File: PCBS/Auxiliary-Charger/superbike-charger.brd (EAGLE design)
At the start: 100 x 80 mm, 20 parts, among them U1 BQ24125RHLR

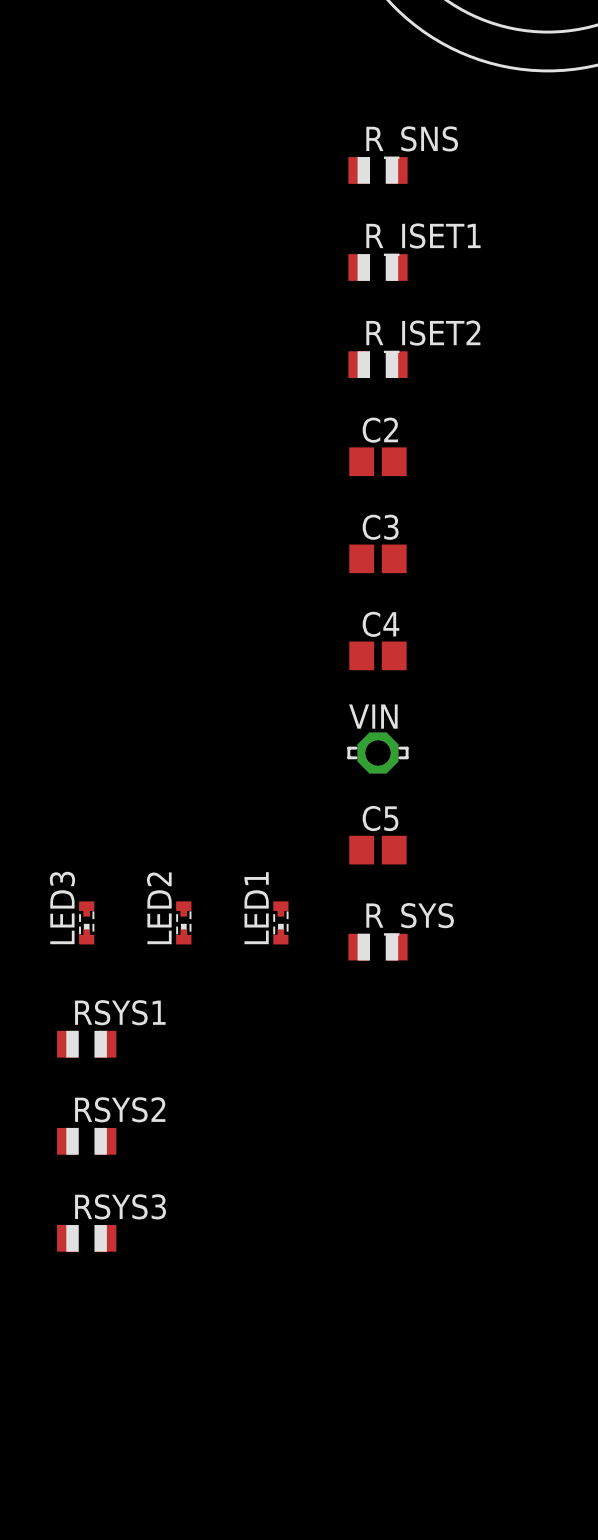
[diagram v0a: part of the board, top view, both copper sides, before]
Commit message: teensy board final draft
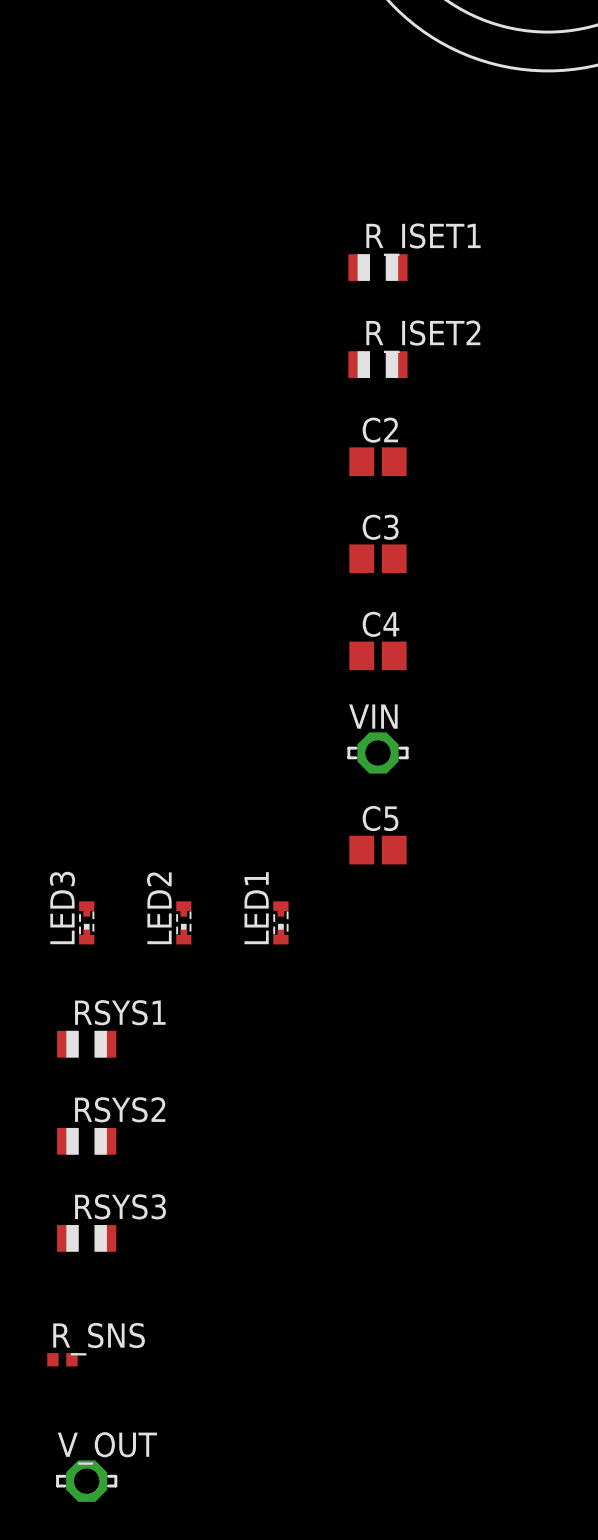
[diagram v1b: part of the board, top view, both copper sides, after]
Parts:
- removed R_SYS: (no value), adafruit:R0805
- added V_OUT: LSP13, solpad:LSP13
- R_SNS: value .05R -> .05; device adafruit:R0805 -> rcl:R0402
- moved R_SNS 64.4 mm to (-36.8, -91.4)
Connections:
- net GND: no longer R_SYS.2
- net N$3: now also R_SNS.2, V_OUT.MP; no longer R_SNS.1, R_SYS.1
- net N$7: now also R_SNS.1; no longer R_SNS.2
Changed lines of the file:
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@@
 <layers>
 <layer number="1" name="Top" color="4" fill="1" visible="yes" active="yes"/>
+<layer number="2" name="Route2" color="1" fill="3" visible="no" active="no"/>
+<layer number="3" name="Route3" color="4" fill="3" visible="no" active="no"/>
+<layer number="4" name="Route4" color="1" fill="4" visible="no" active="no"/>
+<layer number="5" name="Route5" color="4" fill="4" visible="no" active="no"/>
+<layer number="6" name="Route6" color="1" fill="8" visible="no" active="no"/>
+<layer number="7" name="Route7" color="4" fill="8" visible="no" active="no"/>
+<layer number="8" name="Route8" color="1" fill="2" visible="no" active="no"/>
+<layer number="9" name="Route9" color="4" fill="2" visible="no" active="no"/>
+<layer number="10" name="Route10" color="1" fill="7" visible="no" active="no"/>
+<layer number="11" name="Route11" color="4" fill="7" visible="no" active="no"/>
+<layer number="12" name="Route12" color="1" fill="5" visible="no" active="no"/>
+<layer number="13" name="Route13" color="4" fill="5" visible="no" active="no"/>
+<layer number="14" name="Route14" color="1" fill="6" visible="no" active="no"/>
+<layer number="15" name="Route15" color="4" fill="6" visible="no" active="no"/>
 <layer number="16" name="Bottom" color="1" fill="1" visible="yes" active="yes"/>
 <layer number="17" name="Pads" color="2" fill="1" visible="yes" active="yes"/>
@@
 <attribute name="VALUE" x="-16.51" y="-17.78" size="1.27" layer="27" ratio="10"/>
 </element>
-<element name="R_SNS" library="adafruit" library_urn="urn:adsk.eagle:library:420" package="R0805" package3d_urn="urn:adsk.eagle:package:6240566/1" value=".05R" x="-20.32" y="-29.21" smashed="yes">
-<attribute name="NAME" x="-21.082" y="-28.194" size="1.27" layer="25"/>
-<attribute name="VALUE" x="-21.082" y="-31.496" size="1.27" layer="27"/>
-</element>
 <element name="R_ISET1" library="adafruit" library_urn="urn:adsk.eagle:library:420" package="R0805" package3d_urn="urn:adsk.eagle:package:6240566/1" value="10kR" x="-20.32" y="-34.29" smashed="yes">
 <attribute name="NAME" x="-21.082" y="-33.274" size="1.27" layer="25"/>
@@
 <attribute name="VALUE" x="-21.209" y="-67.056" size="1.27" layer="27"/>
 </element>
-<element name="R_SYS" library="adafruit" library_urn="urn:adsk.eagle:library:420" package="R0805" package3d_urn="urn:adsk.eagle:package:6240566/1" value="" x="-20.32" y="-69.85" smashed="yes">
-<attribute name="NAME" x="-21.082" y="-68.834" size="1.27" layer="25"/>
-<attribute name="VALUE" x="-21.082" y="-72.136" size="1.27" layer="27"/>
-</element>
 <element name="LED1" library="adafruit" library_urn="urn:adsk.eagle:library:420" package="SMARTLED-TTW" package3d_urn="urn:adsk.eagle:package:6240563/1" value="" x="-25.4" y="-68.58" smashed="yes">
 <attribute name="NAME" x="-26.035" y="-69.85" size="1.27" layer="25" rot="R90"/>
@@
 <attribute name="NAME" x="-36.322" y="-84.074" size="1.27" layer="25"/>
 <attribute name="VALUE" x="-36.322" y="-87.376" size="1.27" layer="27"/>
+</element>
+<element name="R_SNS" library="rcl" library_urn="urn:adsk.eagle:library:334" package="R0402" package3d_urn="urn:adsk.eagle:package:23547/3" value=".05" x="-36.83" y="-91.44" smashed="yes">
+<attribute name="NAME" x="-37.465" y="-90.805" size="1.27" layer="25"/>
+<attribute name="POPULARITY" value="34" x="-36.83" y="-91.44" size="1.778" layer="27" display="off"/>
+<attribute name="SPICEPREFIX" value="R" x="-36.83" y="-91.44" size="1.778" layer="27" display="off"/>
+<attribute name="VALUE" x="-37.465" y="-93.345" size="1.27" layer="27"/>
+</element>
+<element name="V_OUT" library="solpad" library_urn="urn:adsk.eagle:library:364" package="LSP13" package3d_urn="urn:adsk.eagle:package:26509/1" value="LSP13" x="-35.56" y="-97.79" smashed="yes">
+<attribute name="NAME" x="-37.084" y="-96.52" size="1.27" layer="25" ratio="10"/>
+<attribute name="POPULARITY" value="5" x="-35.56" y="-97.79" size="1.778" layer="27" display="off"/>
+<attribute name="VALUE" x="-35.56" y="-97.536" size="0.0254" layer="27"/>
 </element>
 </elements>
@@
 <contactref element="L_OUT" pad="1"/>
 <contactref element="C_OUT" pad="1"/>
-<contactref element="R_SNS" pad="1"/>
 <contactref element="U1" pad="15"/>
 <contactref element="C2" pad="1"/>
-<contactref element="R_SYS" pad="1"/>
-<wire x1="-21.17" y1="-44.45" x2="-21.32" y2="-69.85" width="0" layer="19" extent="1-1"/>
-<wire x1="-21.32" y1="-29.21" x2="-21.17" y2="-44.45" width="0" layer="19" extent="1-1"/>
-<wire x1="1.69" y1="-24.13" x2="-21.32" y2="-29.21" width="0" layer="19" extent="1-1"/>
+<contactref element="R_SNS" pad="2"/>
+<contactref element="V_OUT" pad="MP"/>
+<wire x1="-36.33" y1="-91.44" x2="-35.56" y2="-97.79" width="0" layer="19" extent="1-1"/>
+<wire x1="-21.17" y1="-44.45" x2="-36.33" y2="-91.44" width="0" layer="19" extent="1-1"/>
+<wire x1="1.69" y1="-24.13" x2="-21.17" y2="-44.45" width="0" layer="19" extent="1-1"/>
 <wire x1="1.04" y1="-12.7" x2="1.69" y2="-24.13" width="0" layer="19" extent="1-1"/>
 <wire x1="5.535" y1="-5.33" x2="1.04" y2="-12.7" width="0" layer="19" extent="1-1"/>
@@
 <contactref element="C4" pad="2"/>
 <contactref element="C5" pad="2"/>
-<contactref element="R_SYS" pad="2"/>
 <contactref element="U1" pad="10"/>
 <contactref element="U1" pad="16"/>
 <contactref element="R_ISET1" pad="1"/>
 <contactref element="12.6V" pad="-"/>
-<wire x1="-19.47" y1="-64.77" x2="-19.32" y2="-69.85" width="0" layer="19" extent="1-1"/>
 <wire x1="-19.47" y1="-54.61" x2="-19.47" y2="-64.77" width="0" layer="19" extent="1-1"/>
 <wire x1="-19.47" y1="-49.53" x2="-19.47" y2="-54.61" width="0" layer="19" extent="1-1"/>
@@
 <contactref element="U1" pad="14"/>
 <contactref element="12.6V" pad="+"/>
-<contactref element="R_SNS" pad="2"/>
-<wire x1="-11.43" y1="-12.7" x2="-19.32" y2="-29.21" width="0" layer="19" extent="1-1"/>
+<contactref element="R_SNS" pad="1"/>
+<wire x1="-11.43" y1="-12.7" x2="-37.33" y2="-91.44" width="0" layer="19" extent="1-1"/>
 <wire x1="5.535" y1="-5.83" x2="-11.43" y2="-12.7" width="0" layer="19" extent="1-1"/>
 </signal>
